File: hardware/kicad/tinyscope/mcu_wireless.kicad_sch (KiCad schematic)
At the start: 13 parts, among them J4 MDBT50Q_TAG_CONNECT, Q2 NMOS, U11 MDBT50Q-1MV2, X1 32k768

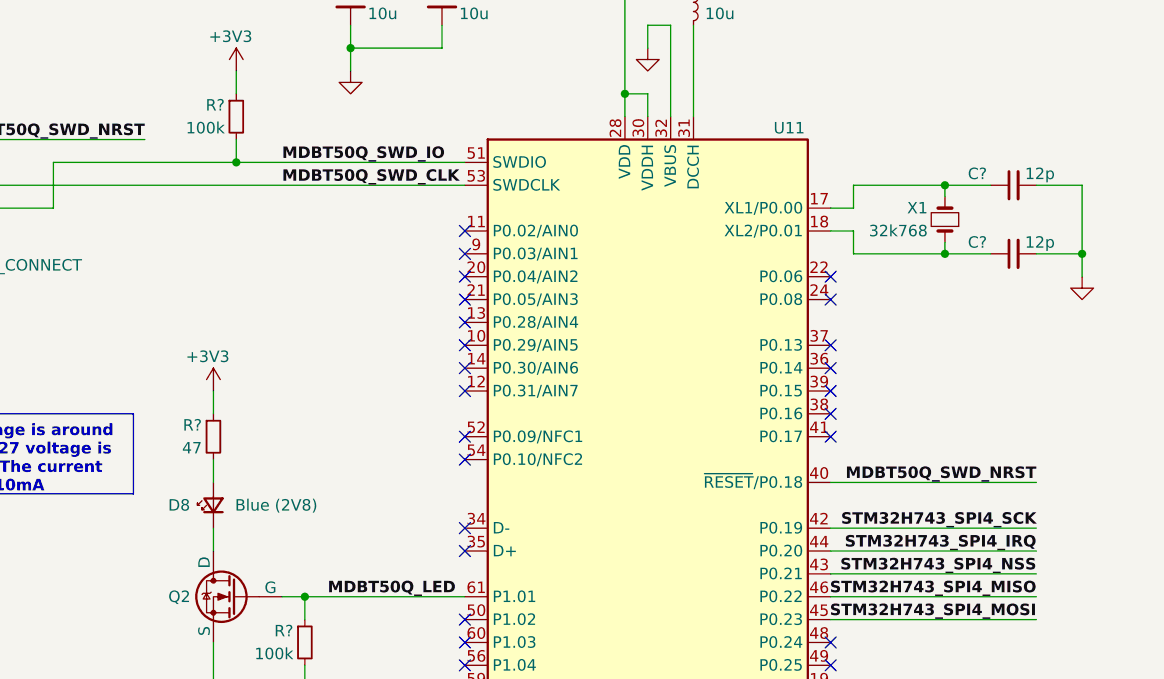
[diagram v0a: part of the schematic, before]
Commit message: feat: hardware: Adds Waveshare 16498 display 02x17 connector. Cleans up all schematics
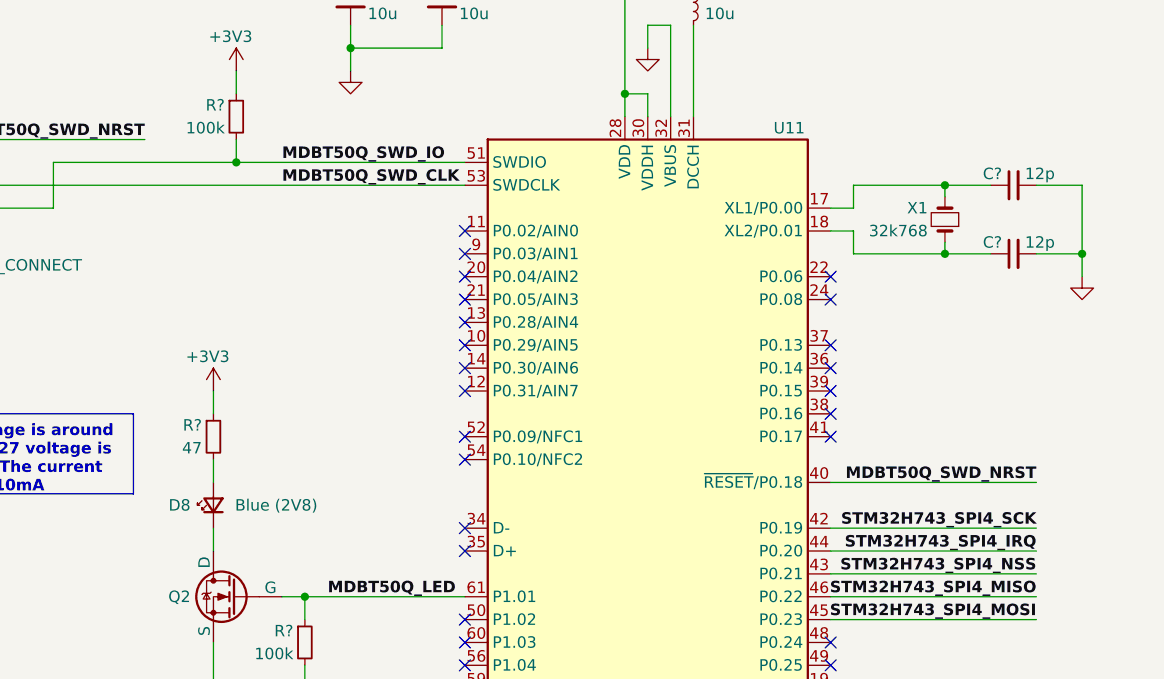
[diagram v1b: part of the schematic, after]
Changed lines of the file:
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@@
   (symbol (lib_id "Device:C_Small") (at 200.66 63.5 90) (mirror x) (unit 1)
     (in_bom yes) (on_board yes) (dnp no)
-    (property "Reference" "C?" (at 195.58 62.23 90)
-      (effects (font (size 1.27 1.27)) (justify right))
+    (property "Reference" "C?" (at 199.39 62.23 90)
+      (effects (font (size 1.27 1.27)) (justify left))
     )
     (property "Value" "12p" (at 201.93 62.23 90)
@@
   (symbol (lib_id "Device:LED_Small") (at 111.76 99.06 90) (unit 1)
     (in_bom yes) (on_board yes) (dnp no)
-    (property "Reference" "D8" (at 107.95 99.06 90)
-      (effects (font (size 1.27 1.27)))
+    (property "Reference" "D8" (at 109.22 99.06 90)
+      (effects (font (size 1.27 1.27)) (justify left))
     )
     (property "Value" "Blue (2V8)" (at 118.745 99.06 90)
@@
   (symbol (lib_id "Device:C_Small") (at 200.66 71.12 90) (mirror x) (unit 1)
     (in_bom yes) (on_board yes) (dnp no)
-    (property "Reference" "C?" (at 195.58 69.85 90)
-      (effects (font (size 1.27 1.27)) (justify right))
+    (property "Reference" "C?" (at 199.39 69.85 90)
+      (effects (font (size 1.27 1.27)) (justify left))
     )
     (property "Value" "12p" (at 201.93 69.85 90)

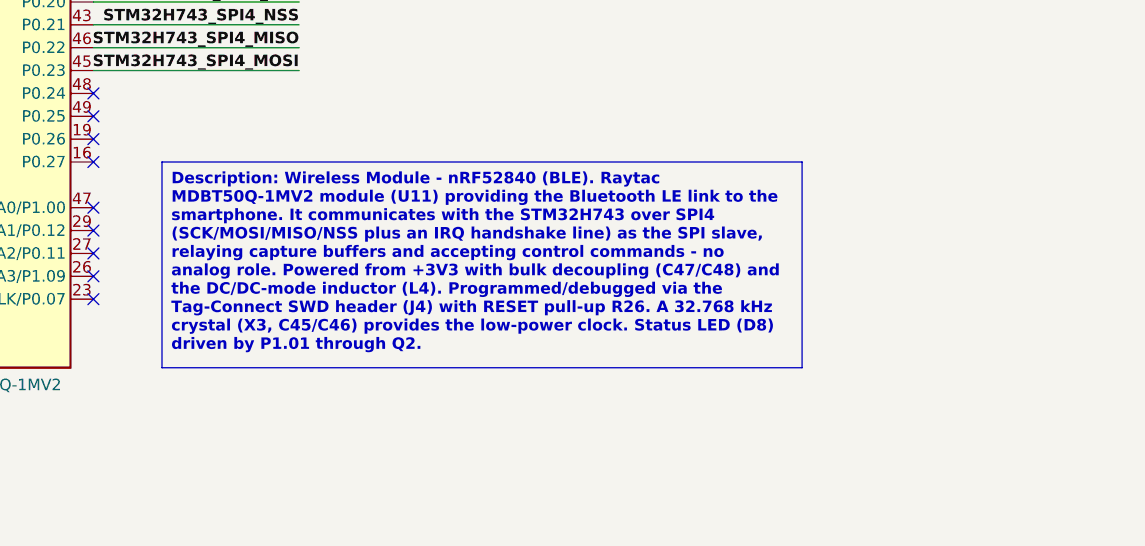
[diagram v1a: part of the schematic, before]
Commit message: feat: hardware: doc: Modifies placement for the schematic description
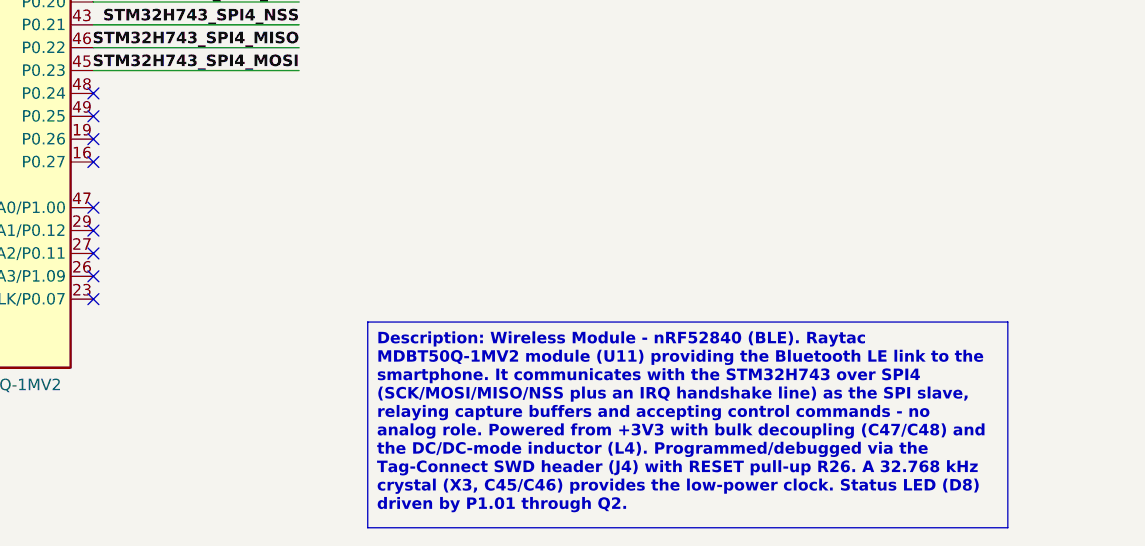
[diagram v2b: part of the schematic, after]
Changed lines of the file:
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@@
   )
   (text_box "Description: Wireless Module - nRF52840 (BLE). Raytac MDBT50Q-1MV2 module (U11) providing the Bluetooth LE link to the smartphone. It communicates with the STM32H743 over SPI4 (SCK/MOSI/MISO/NSS plus an IRQ handshake line) as the SPI slave, relaying capture buffers and accepting control commands - no analog role. Powered from +3V3 with bulk decoupling (C47/C48) and the DC/DC-mode inductor (L4). Programmed/debugged via the Tag-Connect SWD header (J4) with RESET pull-up R26. A 32.768 kHz crystal (X3, C45/C46) provides the low-power clock. Status LED (D8) driven by P1.01 through Q2."
-    (at 187.96 121.92 0) (size 71.12 22.86)
+    (at 210.82 139.7 0) (size 71.12 22.86)
     (stroke (width 0) (type default))
     (fill (type color) (color 255 255 194 1))

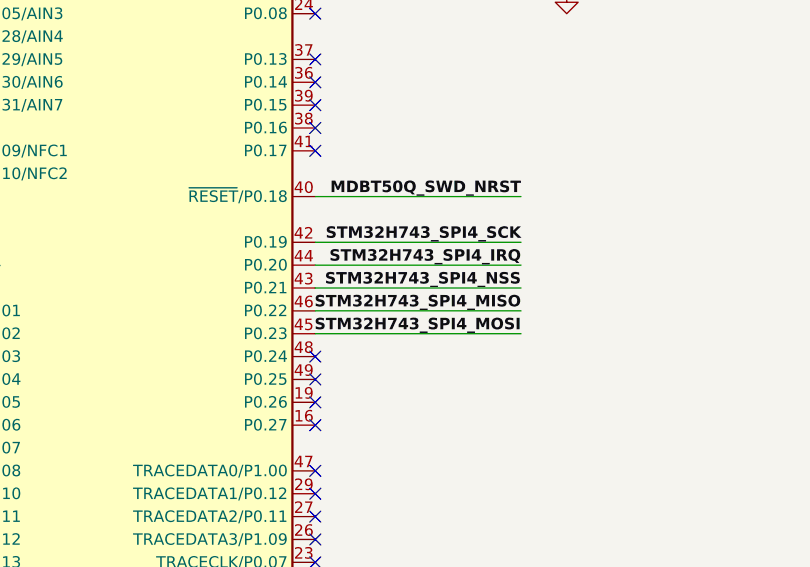
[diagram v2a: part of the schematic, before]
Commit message: fix: hardware: Solves electrical rules warnings and errors #3
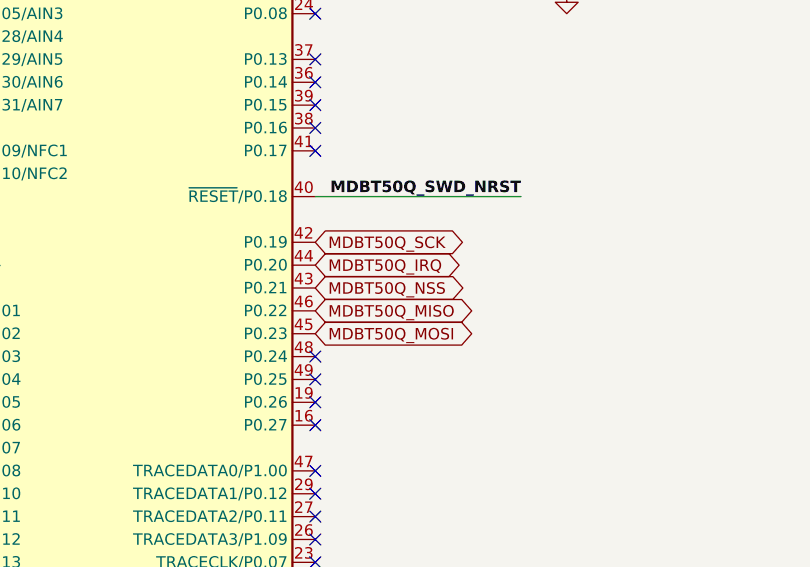
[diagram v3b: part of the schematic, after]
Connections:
- net STM32H743_SPI4_IRQ renamed MDBT50Q_IRQ
- net STM32H743_SPI4_MISO renamed MDBT50Q_MISO
- net STM32H743_SPI4_MOSI renamed MDBT50Q_MOSI
- net STM32H743_SPI4_NSS renamed MDBT50Q_NSS
- net STM32H743_SPI4_SCK renamed MDBT50Q_SCK
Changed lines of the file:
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@@
-    (stroke (width 0) (type default))
-  )
-  (wire (pts (xy 180.34 111.76) (xy 203.2 111.76))
     (stroke (width 0) (type default))
   )
@@
     (stroke (width 0) (type default))
   )
-  (wire (pts (xy 180.34 106.68) (xy 203.2 106.68))
-    (stroke (width 0) (type default))
-  )
   (wire (pts (xy 182.88 68.58) (xy 182.88 71.12))
     (stroke (width 0) (type default))
@@
     (stroke (width 0) (type default))
   )
-  (wire (pts (xy 180.34 101.6) (xy 203.2 101.6))
-    (stroke (width 0) (type default))
-  )
   (wire (pts (xy 114.3 50.8) (xy 114.3 53.34))
     (stroke (width 0) (type default))
@@
     (stroke (width 0) (type default))
   )
-  (wire (pts (xy 180.34 104.14) (xy 203.2 104.14))
-    (stroke (width 0) (type default))
-  )
   (wire (pts (xy 157.48 38.1) (xy 165.1 38.1))
     (stroke (width 0) (type default))
@@
   )
   (wire (pts (xy 127 35.56) (xy 127 38.1))
-    (stroke (width 0) (type default))
-  )
-  (wire (pts (xy 180.34 109.22) (xy 203.2 109.22))
     (stroke (width 0) (type default))
   )
@@
     (effects (font (size 1.27 1.27) (thickness 0.254) bold) (justify left top))
   )
-  (label "STM32H743_SPI4_MISO" (at 203.2 109.22 180) (fields_autoplaced)
-    (effects (font (size 1.27 1.27) bold) (justify right bottom))
-  )
-  (label "STM32H743_SPI4_SCK" (at 203.2 101.6 180) (fields_autoplaced)
-    (effects (font (size 1.27 1.27) bold) (justify right bottom))
-  )
-  (label "STM32H743_SPI4_IRQ" (at 203.2 104.14 180) (fields_autoplaced)
-    (effects (font (size 1.27 1.27) bold) (justify right bottom))
-  )
   (label "MDBT50Q_SWD_IO" (at 119.38 60.96 0) (fields_autoplaced)
     (effects (font (size 1.27 1.27) bold) (justify left bottom))
   )
-  (label "STM32H743_SPI4_NSS" (at 203.2 106.68 180) (fields_autoplaced)
-    (effects (font (size 1.27 1.27) bold) (justify right bottom))
-  )
   (label "MDBT50Q_SWD_CLK" (at 119.38 63.5 0) (fields_autoplaced)
     (effects (font (size 1.27 1.27) bold) (justify left bottom))
   )
-  (label "STM32H743_SPI4_MOSI" (at 203.2 111.76 180) (fields_autoplaced)
-    (effects (font (size 1.27 1.27) bold) (justify right bottom))
-  )
   (label "MDBT50Q_LED" (at 124.46 109.22 0) (fields_autoplaced)
     (effects (font (size 1.27 1.27) bold) (justify left bottom))
@@
     (effects (font (size 1.27 1.27) bold) (justify right bottom))
   )
+  (global_label "MDBT50Q_NSS" (shape bidirectional) (at 180.34 106.68 0) (fields_autoplaced)
+    (effects (font (size 1.27 1.27)) (justify left))
+    (property "Intersheetrefs" "${INTERSHEET_REFS}" (at 197.7827 106.68 0)
+      (effects (font (size 1.27 1.27)) (justify left) hide)
+    )
+  )
+  (global_label "MDBT50Q_MOSI" (shape bidirectional) (at 180.34 111.76 0) (fields_autoplaced)
+    (effects (font (size 1.27 1.27)) (justify left))
+    (property "Intersheetrefs" "${INTERSHEET_REFS}" (at 198.6294 111.76 0)
+      (effects (font (size 1.27 1.27)) (justify left) hide)
+    )
+  )
+  (global_label "MDBT50Q_IRQ" (shape bidirectional) (at 180.34 104.14 0) (fields_autoplaced)
+    (effects (font (size 1.27 1.27)) (justify left))
+    (property "Intersheetrefs" "${INTERSHEET_REFS}" (at 197.2385 104.14 0)
+      (effects (font (size 1.27 1.27)) (justify left) hide)
+    )
+  )
+  (global_label "MDBT50Q_MISO" (shape bidirectional) (at 180.34 109.22 0) (fields_autoplaced)
+    (effects (font (size 1.27 1.27)) (justify left))
+    (property "Intersheetrefs" "${INTERSHEET_REFS}" (at 198.6294 109.22 0)
+      (effects (font (size 1.27 1.27)) (justify left) hide)
+    )
+  )
+  (global_label "MDBT50Q_SCK" (shape bidirectional) (at 180.34 101.6 0) (fields_autoplaced)
+    (effects (font (size 1.27 1.27)) (justify left))
+    (property "Intersheetrefs" "${INTERSHEET_REFS}" (at 197.7827 101.6 0)
+      (effects (font (size 1.27 1.27)) (justify left) hide)
+    )
+  )
   (symbol (lib_id "Device:Crystal_Small") (at 193.04 67.31 90) (unit 1)

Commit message: feat: hardware: Assigns footprints for resistors
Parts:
- R? (x3): footprint (none) -> Resistor_SMD:R_0402_1005Metric
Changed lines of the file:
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@@
       (effects (font (size 1.27 1.27)) (justify right))
     )
-    (property "Footprint" "" (at 114.3 55.88 0)
+    (property "Footprint" "Resistor_SMD:R_0402_1005Metric" (at 114.3 55.88 0)
       (effects (font (size 1.27 1.27)) hide)
     )
@@
       (effects (font (size 1.27 1.27)) (justify right))
     )
-    (property "Footprint" "" (at 111.76 91.44 0)
+    (property "Footprint" "Resistor_SMD:R_0402_1005Metric" (at 111.76 91.44 0)
       (effects (font (size 1.27 1.27)) hide)
     )
@@
       (effects (font (size 1.27 1.27)) (justify right))
     )
-    (property "Footprint" "" (at 121.92 114.3 0)
-      (effects (font (size 1.27 1.27)) hide)
-    )
+    (property "Footprint" "Resistor_SMD:R_0402_1005Metric" (at 121.92 114.3 0)
+      (effects (font (size 1.27 1.27)) hide)
+    )
